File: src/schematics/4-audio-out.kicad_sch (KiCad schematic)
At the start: 34 parts, among them U401 AP22653AW6, U402 MCP6486U, U403 IS31AP4991A-SLS2

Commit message: Some footprint / net bugfixes identified whilst generating the initial PCB.
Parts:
- D401: footprint restall-generic-sot:SOD-323 -> restall-generic-sot:SOD323
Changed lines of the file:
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@@
       (effects (font (size 1.27 1.27)) (justify left))
     )
-    (property "Footprint" "restall-generic-sot:SOD-323" (at 220.98 162.56 0)
+    (property "Footprint" "restall-generic-sot:SOD323" (at 220.98 162.56 0)
       (effects (font (size 1.27 1.27)) (justify right) hide)
     )

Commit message: Started to lay out the PCB.
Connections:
- net GND_PWRIN renamed GND

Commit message: PCB routing.
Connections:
- net AUDIO_SPK_{+} renamed AUDIO_SPK+
- net AUDIO_SPK_{-} renamed AUDIO_SPK-
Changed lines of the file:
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@@
     (effects (font (size 1.27 1.27)) (justify right))
   )
-  (hierarchical_label "AUDIO_SPK_{+}" (shape output) (at 266.7 160.02 0) (fields_autoplaced)
+  (hierarchical_label "AUDIO_SPK+" (shape output) (at 266.7 160.02 0) (fields_autoplaced)
     (effects (font (size 1.27 1.27)) (justify left))
   )
-  (hierarchical_label "AUDIO_SPK_{-}" (shape output) (at 266.7 154.94 0) (fields_autoplaced)
+  (hierarchical_label "AUDIO_SPK-" (shape output) (at 266.7 154.94 0) (fields_autoplaced)
     (effects (font (size 1.27 1.27)) (justify left))
   )

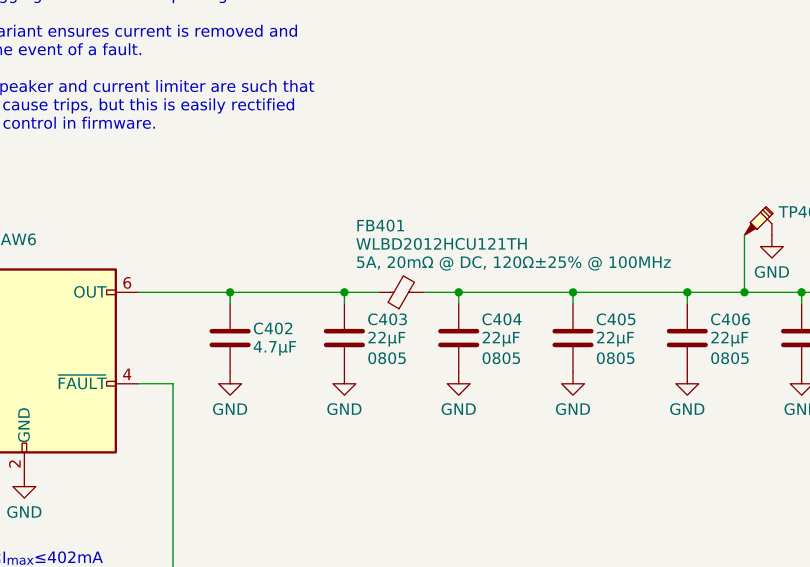
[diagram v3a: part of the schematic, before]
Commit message: PCB routing.  Fixed most of the DRC violations.
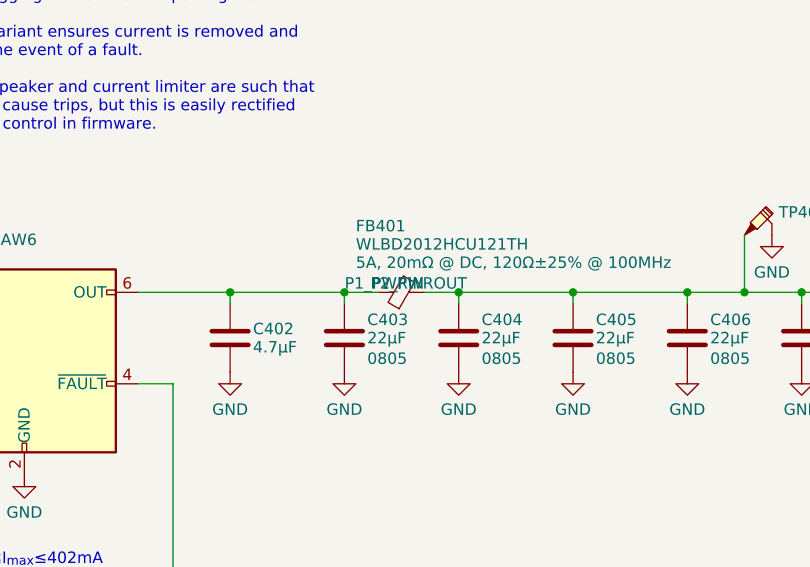
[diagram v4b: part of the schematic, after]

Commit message: Further tweaks, tidy-ups and silkscreen labelling.
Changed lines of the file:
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@@
   (title_block
     (title "MSF Owl Clock - Audio Output Module")
+    (date "June 2024")
     (rev "0.1")
     (company "Pete Restall <pete@restall.net>")

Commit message: Some BOM changes and tweaks found during fab submission.
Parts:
- R406: ManufacturerPartNumber AC0402DR-0716KL -> RC0402FR-0716KL
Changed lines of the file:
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@@
       (effects (font (size 1.27 1.27)) (justify left) hide)
     )
-    (property "ManufacturerPartNumber" "AC0402DR-0716KL" (at 171.45 147.32 0)
+    (property "ManufacturerPartNumber" "RC0402FR-0716KL" (at 171.45 147.32 0)
       (effects (font (size 1.27 1.27)) (justify left) hide)
     )

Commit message: Final push to JLCPCB.  Fixed various component rotation mismatches, some silkscreen issues, BOM amendments due to component availability, etc.
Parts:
- C409, C410: Manufacturer Yageo -> Murata; Manufacturer2 Murata -> Yageo; Manufacturer2PartNumber GCM1885C1H472GA16D -> CC0603FRNPO9BN472; ManufacturerPartNumber CC0603FRNPO9BN472 -> GCM1885C1H472GA16D
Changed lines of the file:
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@@
       (effects (font (size 1.27 1.27)) (justify right))
     )
-    (property "Manufacturer" "Yageo" (at 156.21 152.4 0)
-      (effects (font (size 1.27 1.27)) (justify left) hide)
-    )
-    (property "ManufacturerPartNumber" "CC0603FRNPO9BN472" (at 156.21 152.4 0)
-      (effects (font (size 1.27 1.27)) (justify left) hide)
-    )
-    (property "Manufacturer2" "Murata" (at 156.21 152.4 0)
-      (effects (font (size 1.27 1.27)) (justify left) hide)
-    )
-    (property "Manufacturer2PartNumber" "GCM1885C1H472GA16D" (at 156.21 152.4 0)
+    (property "Manufacturer" "Murata" (at 156.21 152.4 0)
+      (effects (font (size 1.27 1.27)) (justify left) hide)
+    )
+    (property "ManufacturerPartNumber" "GCM1885C1H472GA16D" (at 156.21 152.4 0)
+      (effects (font (size 1.27 1.27)) (justify left) hide)
+    )
+    (property "Manufacturer2" "Yageo" (at 156.21 152.4 0)
+      (effects (font (size 1.27 1.27)) (justify left) hide)
+    )
+    (property "Manufacturer2PartNumber" "CC0603FRNPO9BN472" (at 156.21 152.4 0)
       (effects (font (size 1.27 1.27)) (justify left) hide)
     )
@@
       (effects (font (size 1.27 1.27)) (justify right))
     )
-    (property "Manufacturer" "Yageo" (at 166.37 152.4 0)
-      (effects (font (size 1.27 1.27)) (justify left) hide)
-    )
-    (property "ManufacturerPartNumber" "CC0603FRNPO9BN472" (at 166.37 152.4 0)
-      (effects (font (size 1.27 1.27)) (justify left) hide)
-    )
-    (property "Manufacturer2" "Murata" (at 166.37 152.4 0)
-      (effects (font (size 1.27 1.27)) (justify left) hide)
-    )
-    (property "Manufacturer2PartNumber" "GCM1885C1H472GA16D" (at 166.37 152.4 0)
-      (effects (font (size 1.27 1.27)) (justify left) hide)
-    )
+    (property "Manufacturer" "Murata" (at 166.37 152.4 0)
+      (effects (font (size 1.27 1.27)) (justify left) hide)
+    )
+    (property "ManufacturerPartNumber" "GCM1885C1H472GA16D" (at 166.37 152.4 0)
+      (effects (font (size 1.27 1.27)) (justify left) hide)
+    )
+    (property "Manufacturer2" "Yageo" (at 166.37 152.4 0)
+      (effects (font (size 1.27 1.27)) (justify left) hide)
+    )
+    (property "Manufacturer2PartNumber" "CC0603FRNPO9BN472" (at 166.37 152.4 0)
+      (effects (font (size 1.27 1.27)) (justify left) hide)
+    )
